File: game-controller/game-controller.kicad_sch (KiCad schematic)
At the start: 34 parts, among them SW1 TS-1187A-B-A-B, SW2 TS-1187A-B-A-B, SW3 TS-1187A-B-A-B, SW4 TS-1187A-B-A-B, SW5 TS-1187A-B-A-B, SW6 TS-1187A-B-A-B, SW7 TS-1187A-B-A-B, SW8 TS-1187A-B-A-B, U1 STM32F103C8T6, U2 AP2112K-3.3TRG1, U4 AP2112K-3.3TRG1, X1 TAXM8M4RLBDDT2T

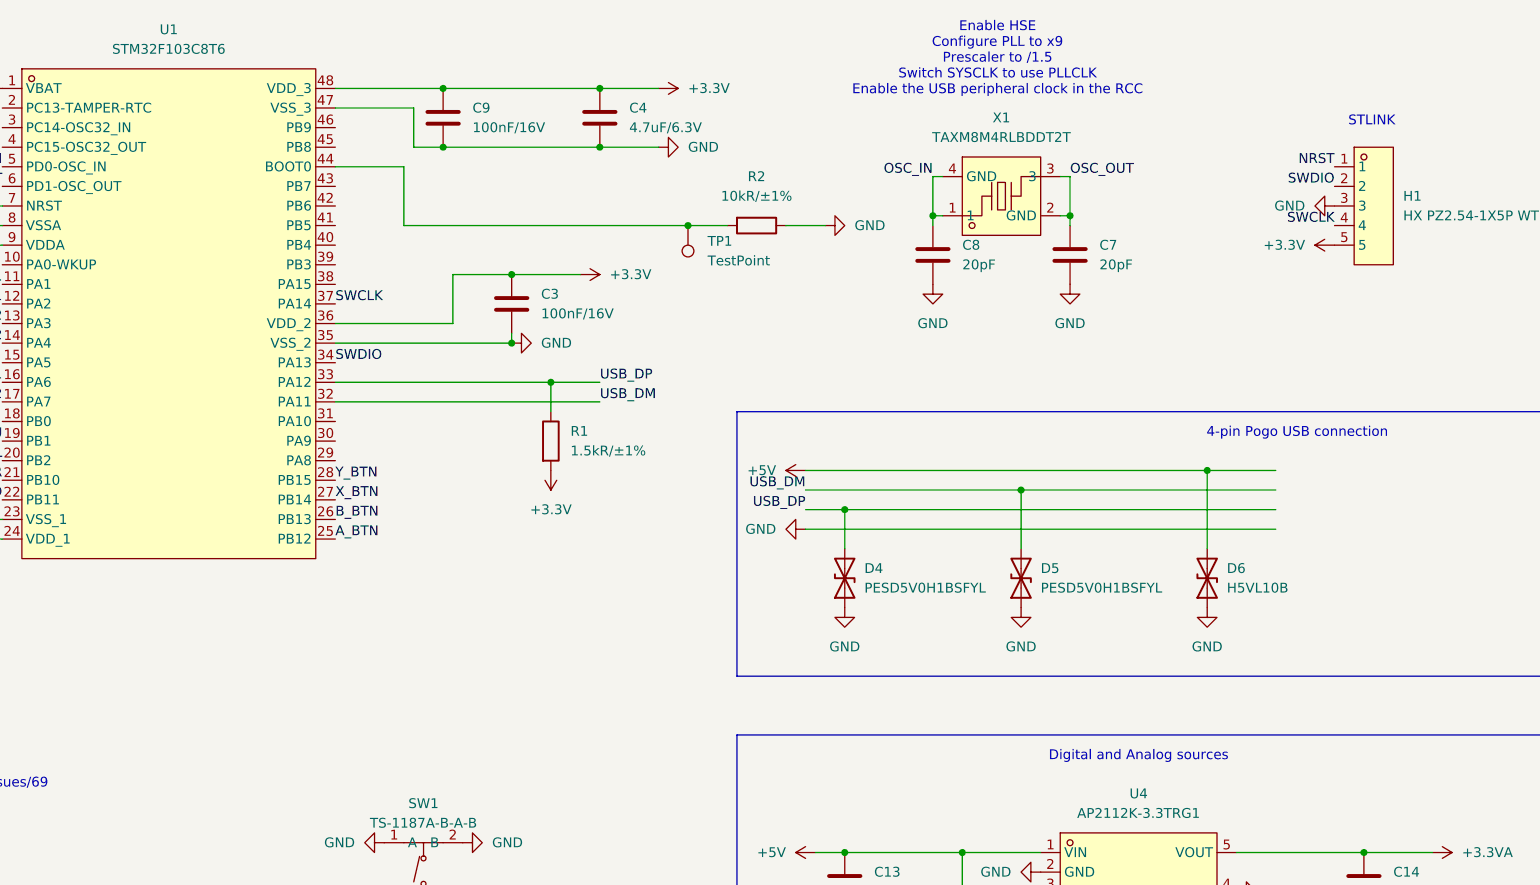
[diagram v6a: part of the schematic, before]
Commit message: Schematics should be done for front board
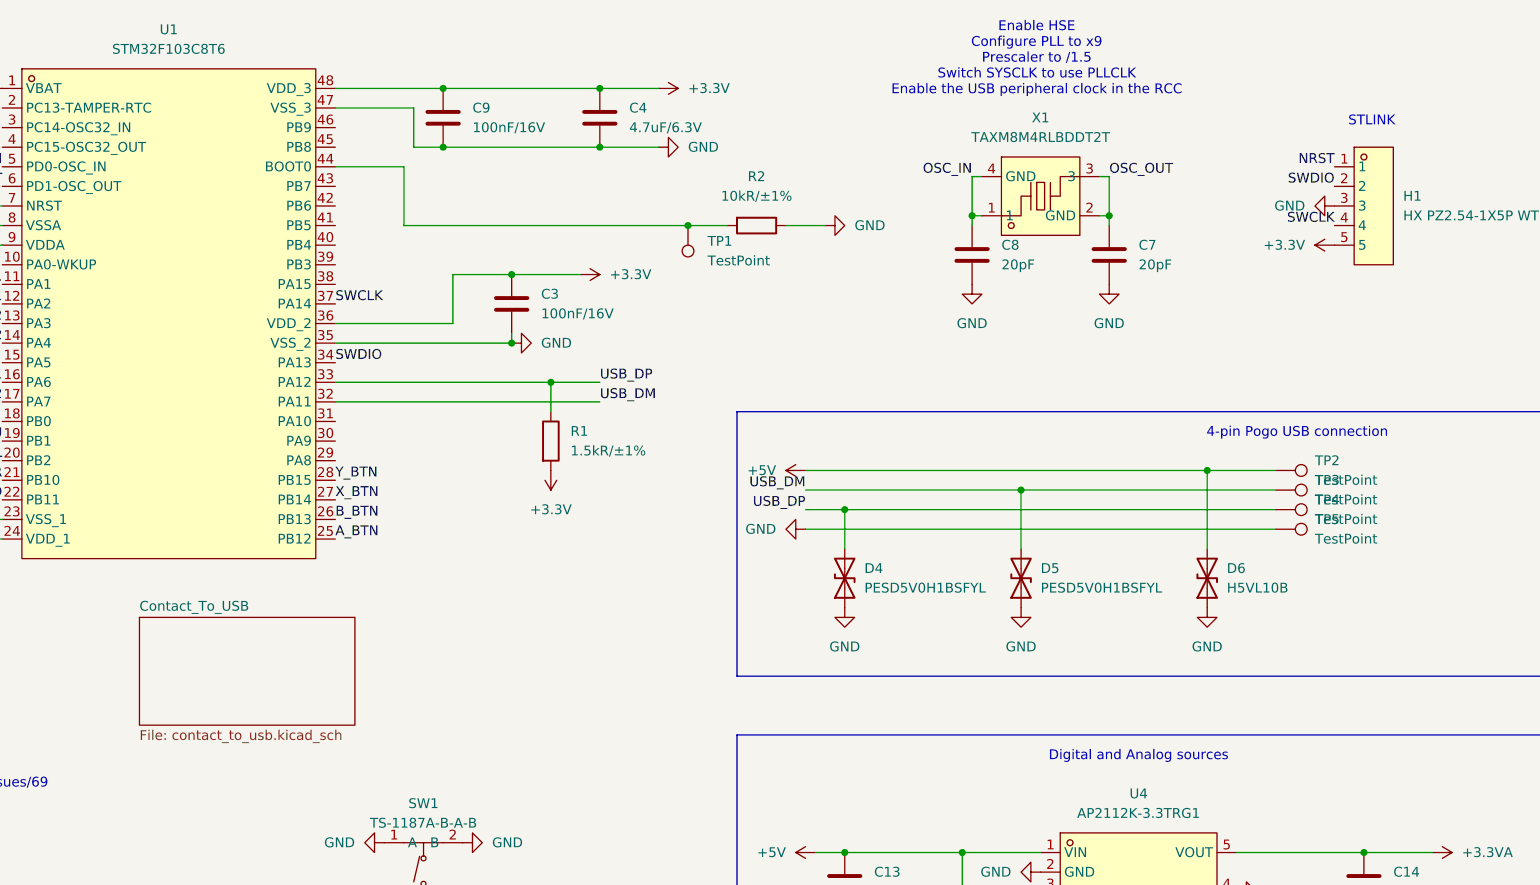
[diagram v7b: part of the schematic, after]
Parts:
- added TP2, TP3, TP4, TP5: TestPoint, TestPoint:TestPoint_Pad_D3.0mm, symbol Connector:TestPoint
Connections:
- net +5V: now also TP2.1
- net GND: now also TP5.1
- net USB_DM: now also TP3.1
- net USB_DP: now also TP4.1
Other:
- added sheet Contact_To_USB (contact_to_usb.kicad_sch)
- moved on the sheet: C7, C8, X1
